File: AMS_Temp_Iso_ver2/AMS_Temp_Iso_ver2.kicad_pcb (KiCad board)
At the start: 2 copper layers, 85 x 117.5 mm, 115 parts, among them J1 Conn_01x02_Pin, J10 Conn_01x02_Pin, J11 Conn_01x02_Pin, J12 Conn_01x02_Pin, J13 Conn_01x10_Socket, J14 Conn_01x04_Pin, J15 Conn_01x04_Pin, J16 Conn_01x04_Pin, J17 Conn_01x04_Pin, J18 Conn_01x02_Pin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

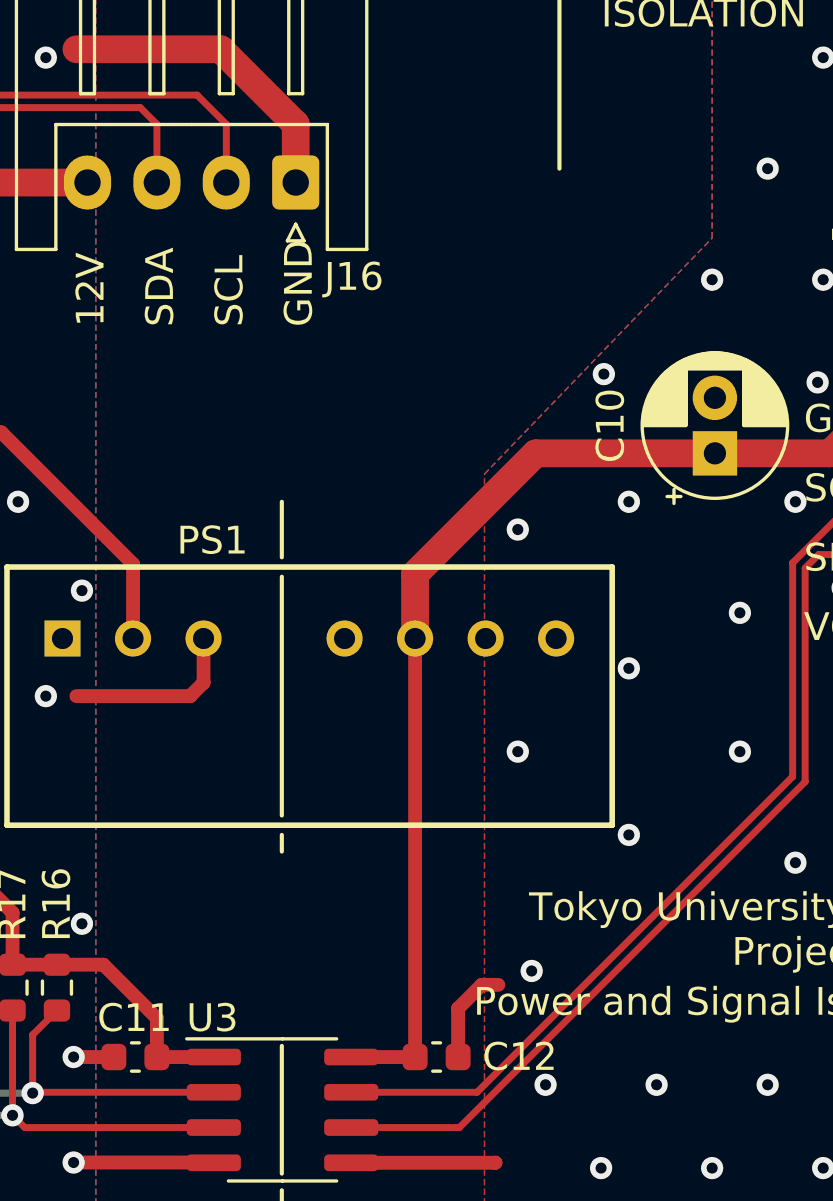
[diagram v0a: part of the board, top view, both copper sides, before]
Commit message: 不要ファイル削除, スリットなし
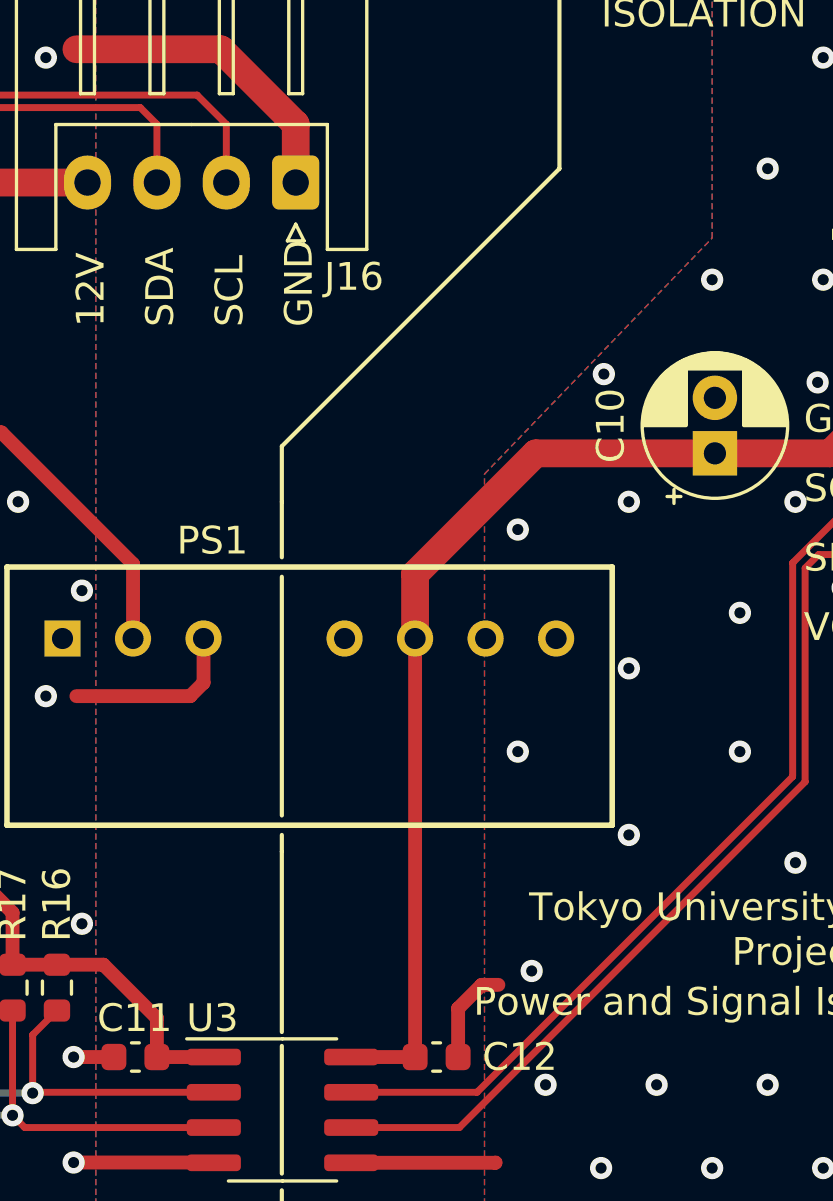
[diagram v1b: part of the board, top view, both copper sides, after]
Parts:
- removed the ? at (141.6, 63.0)
- removed the ? at (136.5, 85.0)
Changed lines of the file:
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@@
       (net 2 "GND"))
   )
-  (footprint "" (layer "F.Cu")
-    (at 141.6 63)
-    (fp_text reference "" (at 0 0) (layer "F.SilkS")
-        (effects (font (size 1.27 1.27) (thickness 0.15)))
-    )
-    (fp_text value "" (at 0 0) (layer "F.SilkS")
-        (effects (font (size 1.27 1.27) (thickness 0.15)))
-    )
-    (pad "" np_thru_hole oval (at 0 0 315) (size 2 15) (drill oval 2 15) (layers "F&B.Cu" "*.Mask"))
-  )
   (footprint "Connector_JST:JST_XH_S4B-XH-A_1x04_P2.50mm_Horizontal" (layer "F.Cu")
     (at 137 57.5 180)
@@
   )
   (footprint "" (layer "F.Cu")
-    (at 136.5 85)
-    (fp_text reference "" (at 0 0) (layer "F.SilkS")
-        (effects (font (size 1.27 1.27) (thickness 0.15)))
-    )
-    (fp_text value "" (at 0 0) (layer "F.SilkS")
-        (effects (font (size 1.27 1.27) (thickness 0.15)))
-    )
-    (pad "" np_thru_hole oval (at 0 0) (size 2 6) (drill oval 2 6) (layers "F&B.Cu" "*.Mask"))
-  )
-  (footprint "" (layer "F.Cu")
     (at 99.75 153.25)
     (fp_text reference "" (at 0 0) (layer "F.SilkS")
@@
   (gr_line (start 136.5 71) (end 136.5 69)
     (stroke (width 0.15) (type default)) (layer "F.SilkS"))
+  (gr_line (start 136.5 67) (end 136.5 69)
+    (stroke (width 0.15) (type default)) (layer "F.SilkS"))
+  (gr_line (start 136.5 88.1) (end 136.5 81.6)
+    (stroke (width 0.15) (type default)) (layer "F.SilkS"))
   (gr_line (start 136.5 97) (end 136.5 93.8)
     (stroke (width 0.15) (type default)) (layer "F.SilkS"))
   (gr_line (start 136.5 93.2) (end 136.5 88.6)
     (stroke (width 0.15) (type default)) (layer "F.SilkS"))
+  (gr_line (start 146.5 57) (end 136.5 67)
+    (stroke (width 0.15) (type default)) (layer "F.SilkS"))
   (gr_line (start 92.5 40) (end 92.5 157.5)
